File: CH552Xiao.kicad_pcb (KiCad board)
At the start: 2 copper layers, 17.8 x 20.3 mm, 19 parts, among them CN1 CON_USB-C-16, J1 Conn_01x07, J2 Conn_01x07, J3 Conn_01x01, J4 Conn_01x01, Q1 TR_NMOS_IRLML6344, SW1 SW_Push, U1 MCU_CH552P

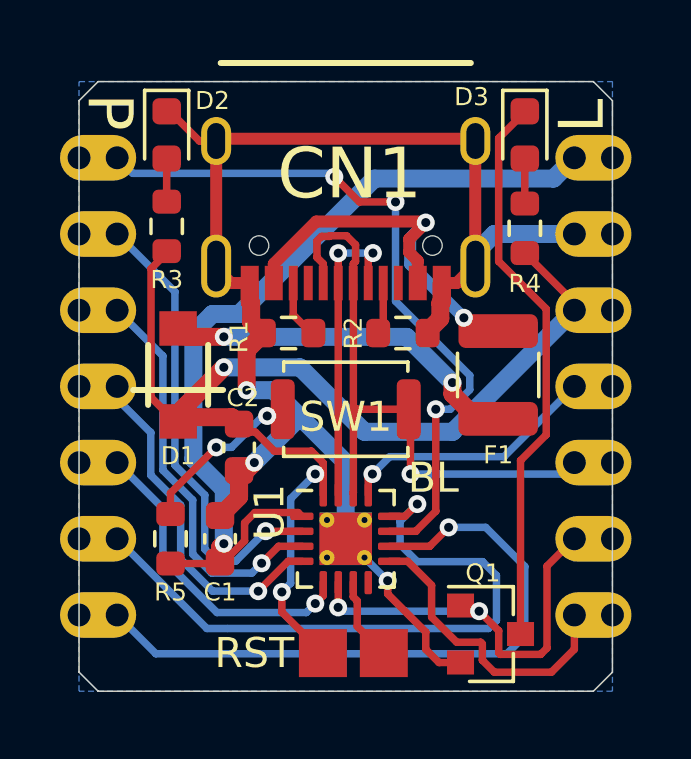
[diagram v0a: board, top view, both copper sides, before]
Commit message: remove vias under USB connector
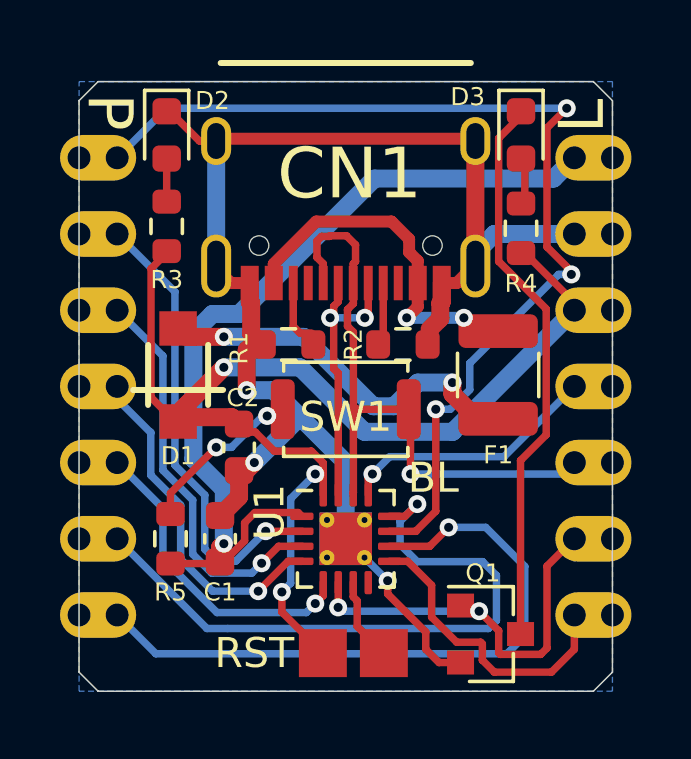
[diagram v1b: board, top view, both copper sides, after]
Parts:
- moved R1 0.38 mm to (6.99, 8.76)
- moved R2 0.38 mm to (10.8, 8.76)
- moved D3 0.13 mm to (14.7, 1.78)
- moved R4 0.13 mm to (14.7, 4.89)
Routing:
- net /P1.1: track 23.8 -> 33.9 mm
- net Net-(CN1-PadA4): track 12.8 -> 10.8 mm
- net /P3.7: track 10.4 -> 9.66 mm
- net Net-(D1-PadA): track 11.8 -> 12.4 mm

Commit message: KiCAD6、CH552T
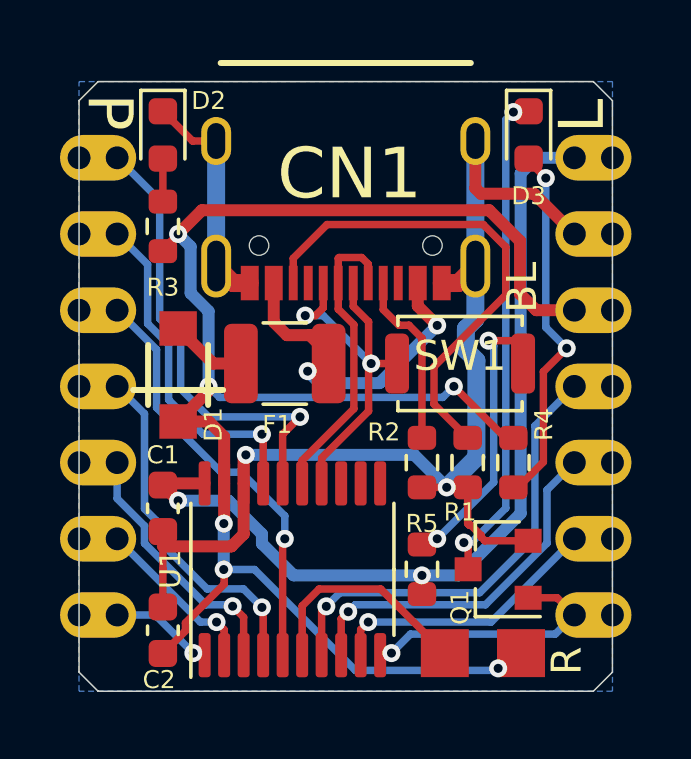
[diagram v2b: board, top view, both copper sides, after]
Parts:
- U1: value MCU_CH552P -> MCU_CH552T; footprint Package_DFN_QFN:QFN-16-1EP_3x3mm_P0.5mm_EP1.75x1.75mm_ThermalVias -> Package_SO:TSSOP-20_4.4x6.5mm_P0.65mm
- moved R5 8.44 mm to (11.4, 16.3)
- moved R4 7.81 mm to (14.5, 12.7), turned to -90 degrees
- moved R1 7.15 mm to (13.0, 12.7), turned to -90 degrees
- moved F1 7.12 mm to (6.86, 9.40), turned to 0 degrees
- moved C2 6.60 mm to (2.79, 18.3), turned to 90 degrees
- moved J3 6.60 mm to (14.7, 19.1)
- moved SW1 4.10 mm to (12.7, 9.40), turned to 0 degrees
- moved R2 3.99 mm to (11.4, 12.7), turned to -90 degrees
- moved Q1 2.17 mm to (14.0, 16.3), turned to 180 degrees
- moved C1 2.16 mm to (2.79, 14.2), turned to -90 degrees
- moved U1 2.05 mm to (7.11, 16.3), turned to 90 degrees
- moved J4 2.03 mm to (12.2, 19.1)
- moved D3 0.25 mm to (15.0, 1.78)
- moved D2 0.13 mm to (2.79, 1.78)
- moved R3 0.13 mm to (2.79, 4.83)
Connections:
- CN1 pad A8: Net-(CN1-PadA8) -> unconnected-(CN1-PadA8)
- CN1 pad B8: Net-(CN1-PadB8) -> unconnected-(CN1-PadB8)
- J1 pad 1: /P1.1 -> /P1.3
- J1 pad 2: /P1.5 -> /P1.2
- J1 pad 3: /P1.4 -> /P1.7
- J1 pad 4: /P3.2 -> /P1.6
- J1 pad 5: /P1.6 -> /P1.5
- J1 pad 6: /P3.3 -> /P1.4
- J1 pad 7: /P3.0 -> /P3.2
- J2 pad -: (no net) -> +3V3
- J2 pad 1: /P3.1 -> /P3.0
- J2 pad 2: /P1.7 -> /P3.1
- J2 pad 3: /P3.6 -> /P1.1
- J2 pad 4: /P3.4 -> /P1.0
- Q1 pad 1: /P1.7 -> /P3.0
- U1 pad 1: +3V3 -> /P3.2
- U1 pad 11: /P1.1 -> /P3.3
- U1 pad 12: /P3.3 -> /P3.4
- U1 pad 13: /P3.4 -> /P3.5
- U1 pad 16: +5V -> /P1.3
- U1 pad 17: GND -> /P1.2
- U1 pad 2: /P1.5 -> /P1.4
- U1 pad 3: /P1.4 -> /P1.5
- U1 pad 4: /P3.2 -> /P1.6
- U1 pad 5: /P1.6 -> /P1.7
- U1 pad 6: /P1.7 -> /RST
- U1 pad 7: /RST -> /P1.0
- U1 pad 8: /P1.0 -> /P1.1
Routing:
- net /P3.3: track 21.8 -> 0.00 mm, vias 1 -> 0
- net /P1.1: track 33.9 -> 12.2 mm, vias 3 -> 1
- net +5V: track 38.4 -> 56.4 mm, vias 3 -> 6
- net /P1.3: track 0.00 -> 15.4 mm, vias 0 -> 1
- net /P1.0: track 0.00 -> 15.2 mm, vias 0 -> 1
- net Net-(CN1-PadB5): track 2.14 -> 16.5 mm
- net /P3.0: track 22.0 -> 8.81 mm
- net /P1.2: track 0.00 -> 11.5 mm, vias 0 -> 1
- net Net-(D3-Pad2): track 1.50 -> 12.3 mm, vias 0 -> 2
- net Net-(D1-PadA): track 12.4 -> 2.58 mm, vias 2 -> 0
- net /P3.4: track 8.69 -> 0.00 mm, vias 1 -> 0
- net /P3.6: track 21.2 -> 12.9 mm, vias 1 -> 2
- net /P3.2: track 11.6 -> 3.47 mm
- net /P1.4: track 13.4 -> 5.67 mm
- net /P1.5: track 15.5 -> 8.66 mm
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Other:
- net class Default removed
- board text added: "1.0"
- board text added: "1.2"
- board text added: "1.3"
- board text added: "1.6"
- board text added: "1.7"
- board text added: "3.0~"
- board text added: "3.1~~"
- board text added: "@akita11"
- board text added: "A1.1"
- board text added: "A1.4"
- board text added: "A3.2"
- board text added: "R"
- board text added: "~A1.5"
- board text removed: "1.1"
- board text removed: "1.5"
- board text removed: "P1.4"
- board text removed: "P1.6"
- board text removed: "P1.7"
- board text removed: "P3.0"
- board text removed: "P3.1"
- board text removed: "P3.2"
- board text removed: "P3.3"
- board text removed: "P3.4"
- board text removed: "P3.6"
- board text removed: "RST"
